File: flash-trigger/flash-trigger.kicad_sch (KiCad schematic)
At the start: 32 parts, among them J1 TRIG, J2 GND, J3 GND, J4 GND, Q1 NDS331N, SW1 PCM12, SW2 Bat Test, U1 74LV123, U2 BD49K27G

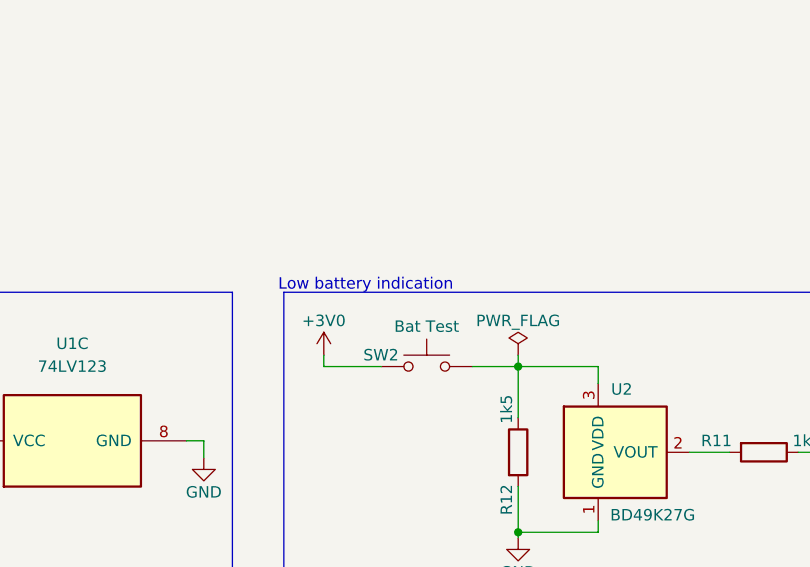
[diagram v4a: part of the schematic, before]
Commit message: schematics: Fix the battery good title
Since rev2 this is now a battery good detection.
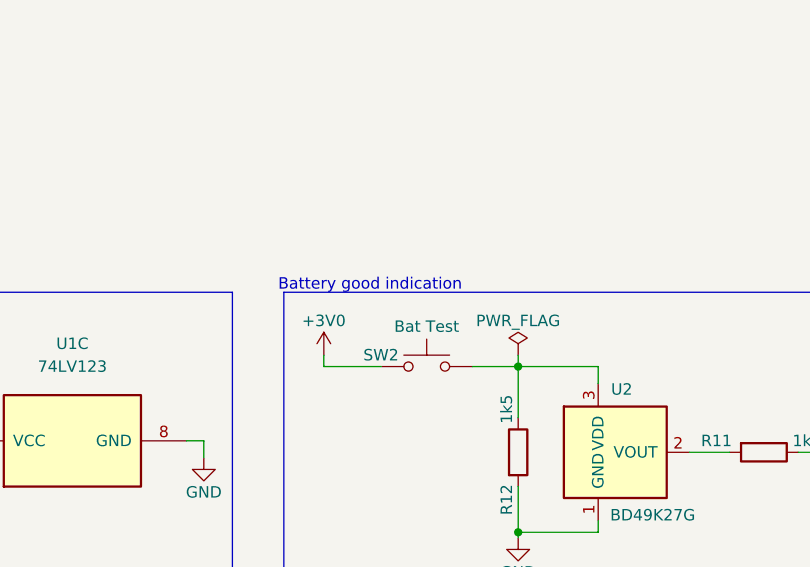
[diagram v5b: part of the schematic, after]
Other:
- note added: "Battery good indication"
- note removed: "Low battery indication"
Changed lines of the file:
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@@
     (effects (font (size 1.27 1.27)) (justify left bottom))
   )
-  (text "Low battery indication" (at 113.665 118.745 0)
+  (text "Battery good indication" (at 113.665 118.745 0)
     (effects (font (size 1.27 1.27)) (justify left bottom))
   )

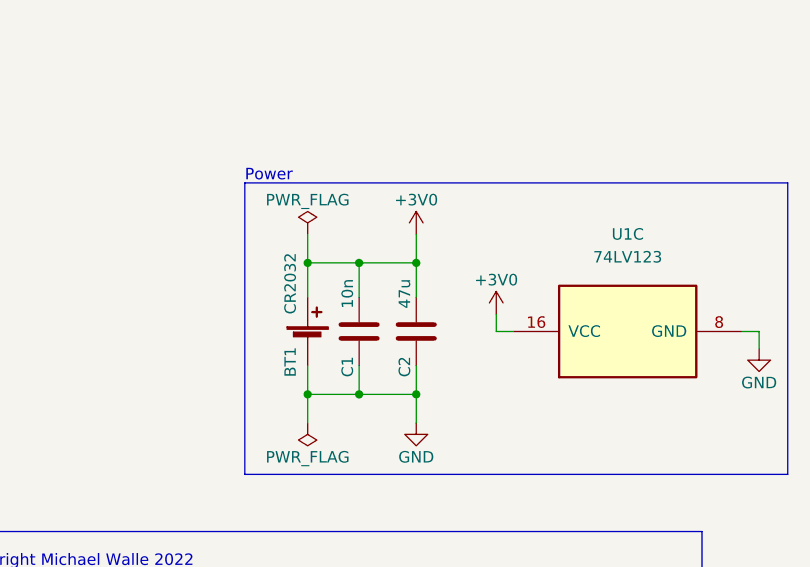
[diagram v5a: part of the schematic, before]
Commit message: flash-trigger: Increase C2 to 100uF
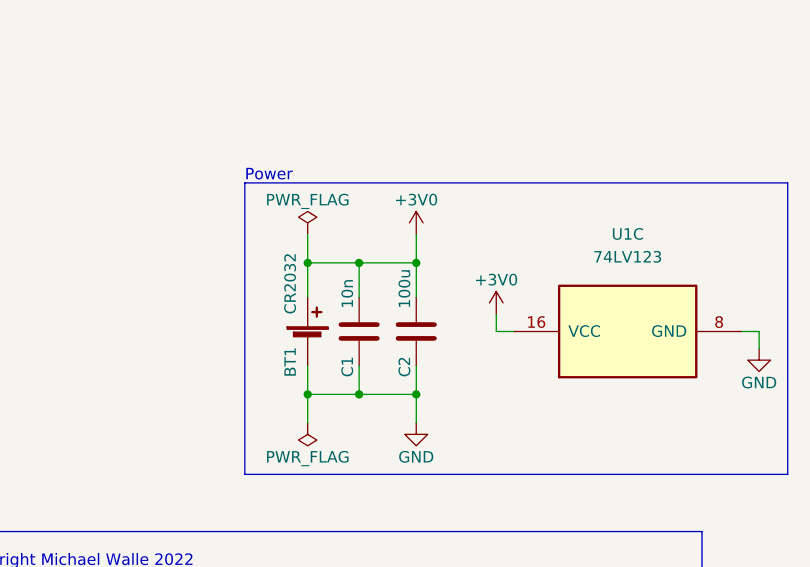
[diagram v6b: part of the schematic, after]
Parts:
- C2: value 47u -> 100u
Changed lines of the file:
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@@
       (effects (font (size 1.27 1.27)) (justify left))
     )
-    (property "Value" "47u" (id 1) (at 66.04 132.715 90)
+    (property "Value" "100u" (id 1) (at 66.04 132.715 90)
       (effects (font (size 1.27 1.27)) (justify left))
     )
@@
     )
     (path "/8eb124df-87e9-488c-9f2f-f3f6fb560814"
-      (reference "C2") (unit 1) (value "47u") (footprint "Capacitor_SMD:C_0805_2012Metric_Pad1.18x1.45mm_HandSolder")
+      (reference "C2") (unit 1) (value "100u") (footprint "Capacitor_SMD:C_0805_2012Metric_Pad1.18x1.45mm_HandSolder")
     )
     (path "/21972450-4e20-4965-b341-d4d19cc02663"

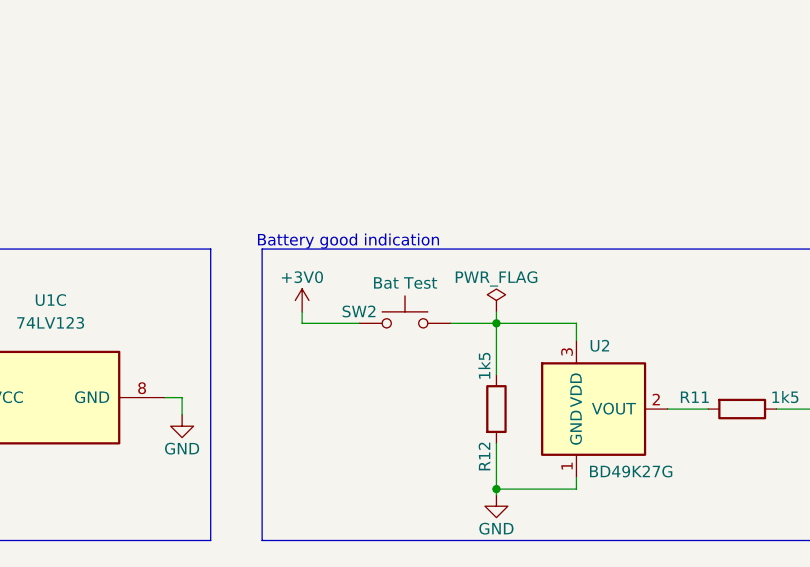
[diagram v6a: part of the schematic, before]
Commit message: flash-trigger: Update value of SW2
Reflect the actual component value instead of its function.
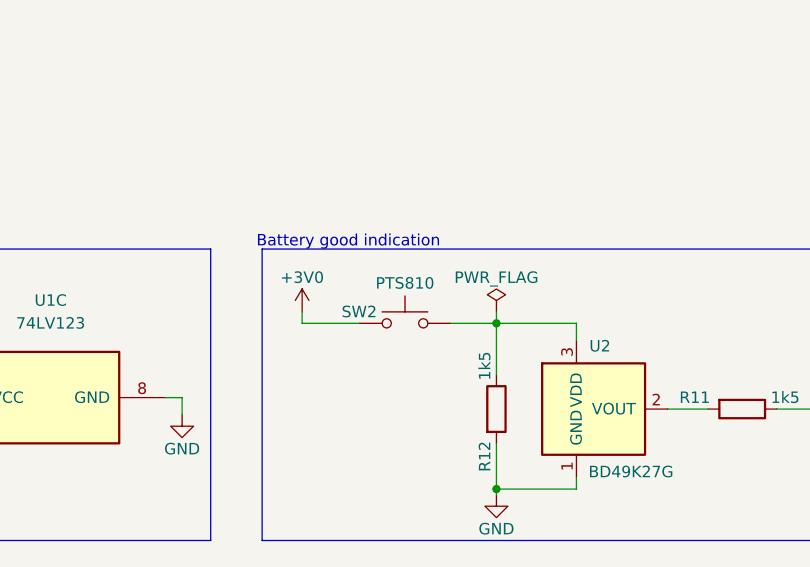
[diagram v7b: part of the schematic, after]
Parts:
- SW2: value Bat Test -> PTS810
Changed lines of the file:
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@@
     (in_bom yes) (on_board yes)
     (property "Reference" "SW2" (id 0) (at 125.095 125.73 0))
-    (property "Value" "Bat Test" (id 1) (at 130.175 122.555 0))
+    (property "Value" "PTS810" (id 1) (at 130.175 122.555 0))
     (property "Footprint" "Button_Switch_CKComponents:SW_SPST_PTS810" (id 2) (at 130.175 121.92 0)
       (effects (font (size 1.27 1.27)) hide)
@@
     )
     (path "/f9b8f20f-45f6-4ac3-a78b-1472384cf738"
-      (reference "SW2") (unit 1) (value "Bat Test") (footprint "Button_Switch_CKComponents:SW_SPST_PTS810")
+      (reference "SW2") (unit 1) (value "PTS810") (footprint "Button_Switch_CKComponents:SW_SPST_PTS810")
     )
     (path "/ede317ec-a3ef-47a7-b8e2-075ff55a0a1f"
